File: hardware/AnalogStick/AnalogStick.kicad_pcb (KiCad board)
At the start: 2 copper layers, 15 x 11.5 mm, 3 parts, among them J1 Conn_01x06

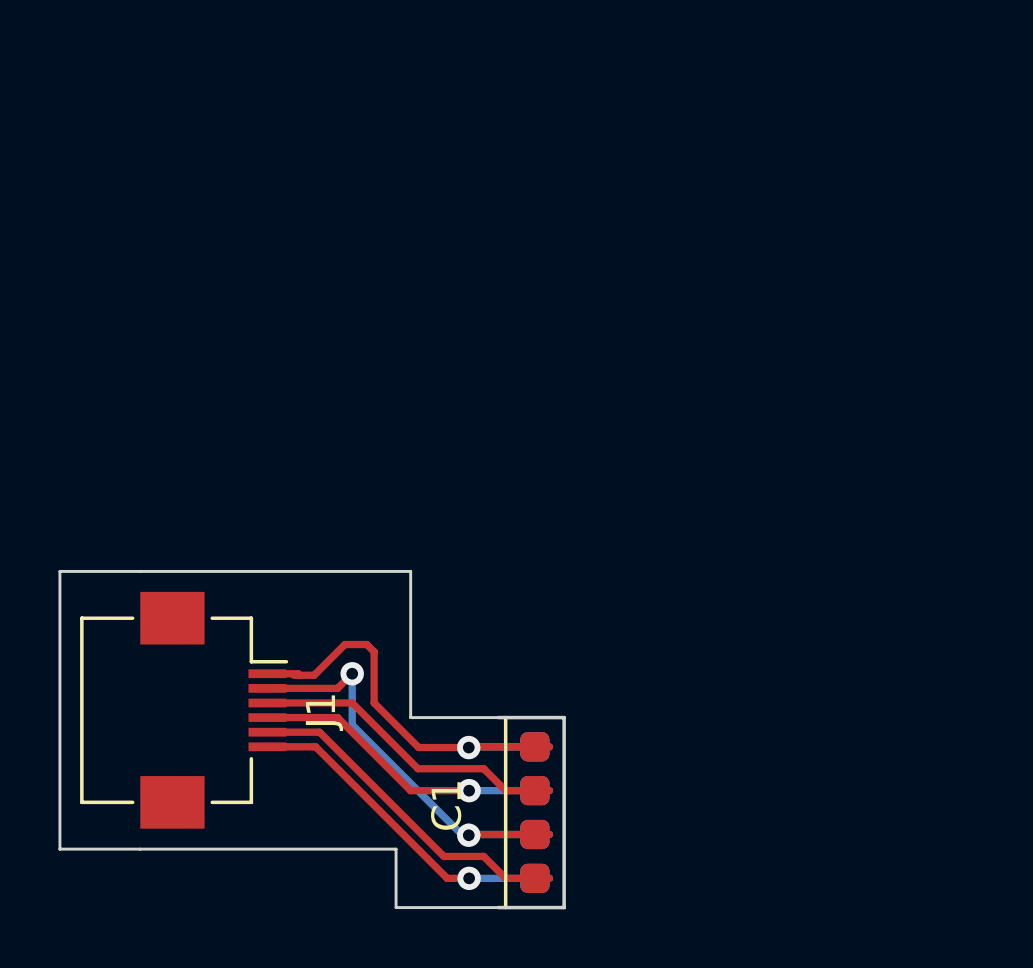
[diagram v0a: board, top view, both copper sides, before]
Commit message: First pass analog stick FPC
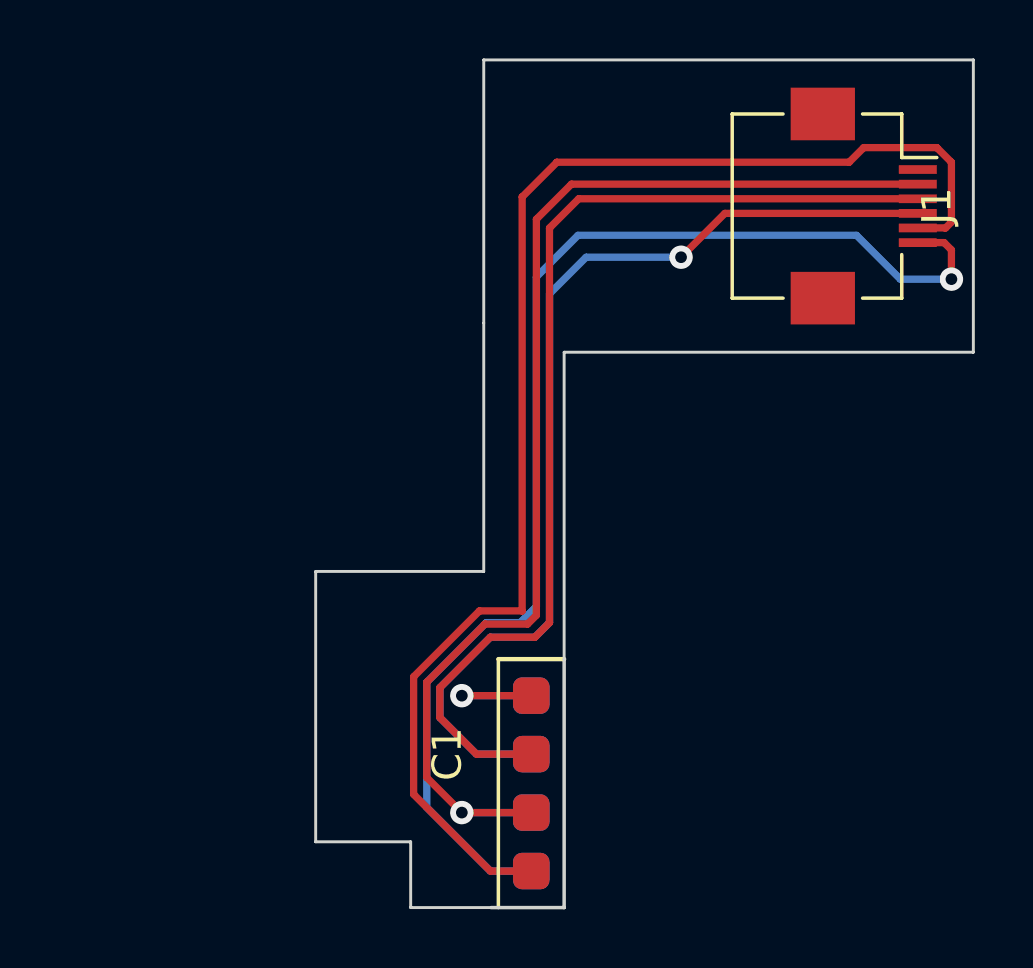
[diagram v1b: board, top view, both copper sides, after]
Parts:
- moved J1 28.2 mm to (152.0, 69.0)
- moved G*** 24.8 mm to (147.2, 69.0)
- moved C1 1.75 mm to (140.8, 88.0)
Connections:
- J1 pad 1: /GND -> unconnected-(J1-Pad1)
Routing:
- net /Y_1: track 11.8 -> 46.8 mm
- net /Y_2: track 11.6 -> 42.5 mm
- net /+v: track 16.3 -> 41.5 mm, vias 2 -> 1
- net /X_1: track 10.9 -> 35.9 mm
- net /X_2: track 10.7 -> 34.3 mm
- net /GND: track 15.6 -> 4.75 mm
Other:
- board size 15 x 11.5 mm -> 22.5 x 29 mm

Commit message: Cleanup and add documentation
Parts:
- removed J1: Conn_01x06, Connector_FFC-FPC:Hirose_FH12-6S-0.5SH_1x06-1MP_P0.50mm_Horizontal
- added TP1: TestPoint, TestPoint:TestPoint_Pad_1.0x1.0mm, F.Cu at (154.2, 65.5)
- added TP2: TestPoint, TestPoint:TestPoint_Pad_1.0x1.0mm, F.Cu at (154.2, 69.0)
- added TP3: TestPoint, TestPoint:TestPoint_Pad_1.0x1.0mm, F.Cu at (154.2, 72.2)
- added TP4: TestPoint, TestPoint:TestPoint_Pad_1.0x1.0mm, F.Cu at (150.8, 67.0)
- added TP5: TestPoint, TestPoint:TestPoint_Pad_1.0x1.0mm, F.Cu at (150.5, 70.8)
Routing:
- net /Y_1: track 46.8 -> 39.1 mm
- net /Y_2: track 42.5 -> 34.8 mm
- net /+v: track 41.5 -> 43.6 mm
- net /X_2: track 34.3 -> 32.5 mm

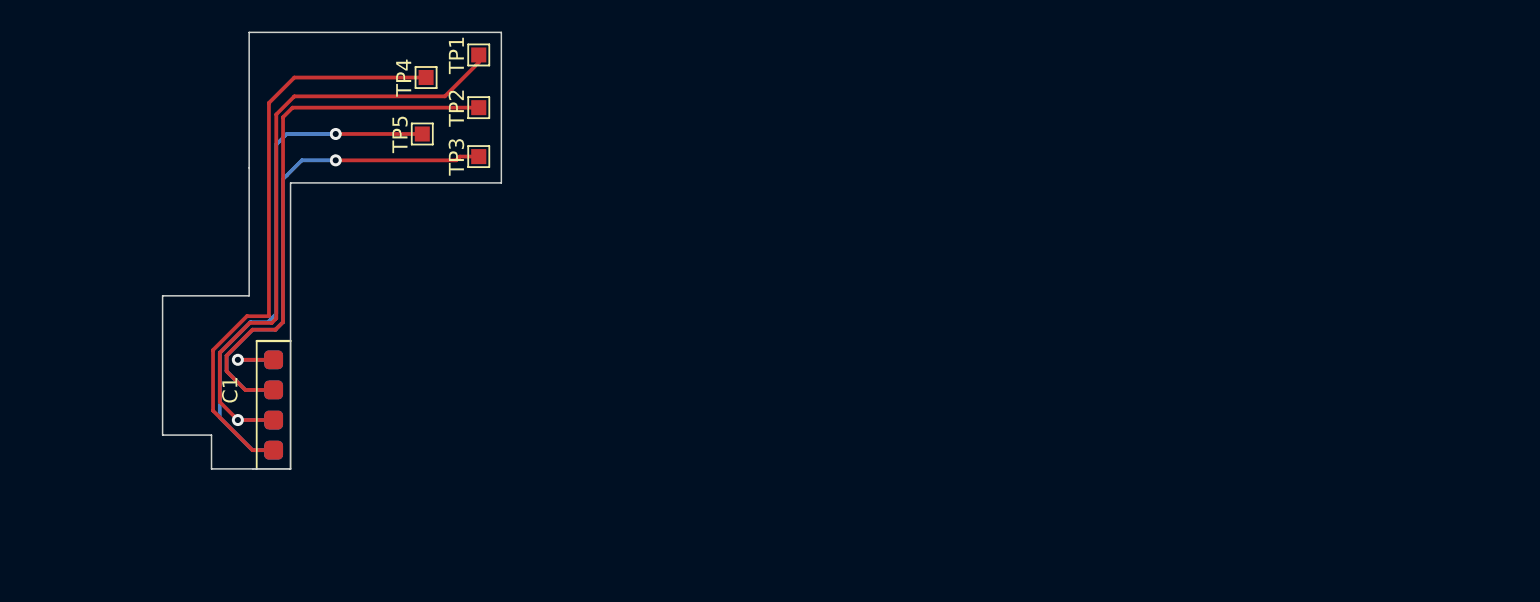
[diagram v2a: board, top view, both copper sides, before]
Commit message: Added analog stick
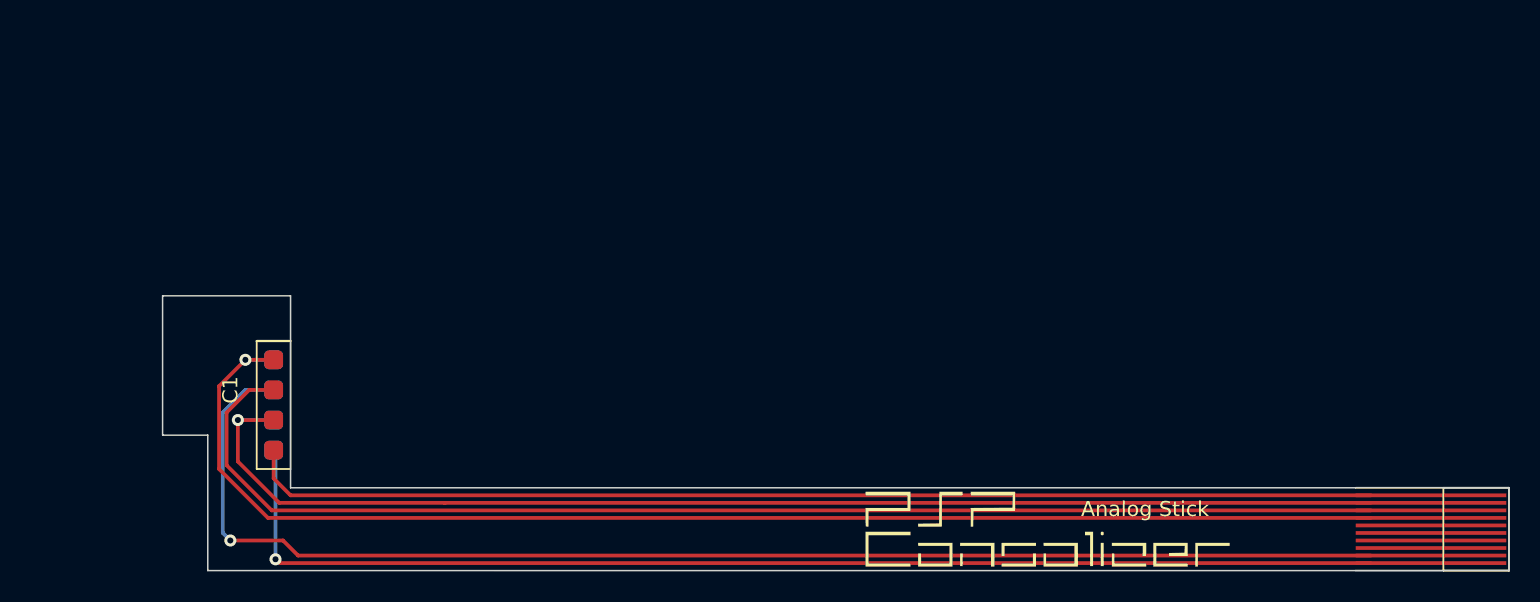
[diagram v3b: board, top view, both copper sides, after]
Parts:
- removed TP1, TP2, TP3, TP4, TP5: TestPoint, TestPoint:TestPoint_Pad_1.0x1.0mm
- added C2: flex-conector_10, consolizer:flex_long_10, F.Cu at (218.5, 97.3)
- added G***: LOGO, consolizer:logo_small, F.Cu at (192.0, 97.0)
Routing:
- net /GND: track 4.75 -> 89.6 mm
- net /X_2: track 32.5 -> 88.9 mm
- net /X_1: track 36.2 -> 84.5 mm
- net /Y_2: track 34.8 -> 80.2 mm
- net /+v: track 43.6 -> 83.9 mm
- net /Y_1: track 39.1 -> 75.2 mm
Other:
- board size 22.5 x 29 mm -> 79.2 x 18.3 mm
- board text added: "Analog Stick"
